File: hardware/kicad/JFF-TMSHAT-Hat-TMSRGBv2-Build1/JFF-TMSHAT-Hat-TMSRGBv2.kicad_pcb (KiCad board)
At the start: 2 copper layers, 56 x 73.5 mm, 15 parts, among them J1 TMSRGB-OUT, J13 AV EXT, J5 RGB, U100 TMS-RGB

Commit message: tmshats: add missing Y,R-Y,B-Y resistors
Signed-off-by: Albert Herranz <albert_herranz@yahoo.es>
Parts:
- added R16: 470, Resistor_SMD:R_0805_2012Metric_Pad1.20x1.40mm_HandSolder, F.Cu at (113.7, 122.5)
- added R17: 470, Resistor_SMD:R_0805_2012Metric_Pad1.20x1.40mm_HandSolder, F.Cu at (113.7, 120.0)
- added R18: 470, Resistor_SMD:R_0805_2012Metric_Pad1.20x1.40mm_HandSolder, F.Cu at (113.7, 127.5)
- moved SYM1 72.0 mm to (67.5, 75.2)
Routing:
- net AUDIO: track 95.5 -> 113.3 mm
- net COMVID/Y: track 35.0 -> 41.5 mm
- net EXTVDP/B-Y: track 35.0 -> 41.6 mm
- net CPUCLK/R-Y: track 44.2 -> 50.4 mm, vias 0 -> 1
- net GND: track 22.4 -> 18.9 mm, vias 2 -> 0

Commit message: tmshats: re-routed for enhanced reference plane
Signed-off-by: Albert Herranz <albert_herranz@yahoo.es>
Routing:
- net AUDIO: track 113.3 -> 83.4 mm, vias 0 -> 1
- net /AV: track 35.9 -> 51.8 mm, vias 1 -> 0
- net GND: track 18.9 -> 32.5 mm, vias 0 -> 7
- net /YS: track 40.1 -> 53.0 mm, vias 1 -> 0
- net +5V: track 65.5 -> 71.1 mm
- net SYNC_75: track 32.3 -> 30.8 mm

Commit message: tmshats: changed logos, minor routing change
Signed-off-by: Albert Herranz <albert_herranz@yahoo.es>
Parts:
- added G***: LOGO, My_Components:logo-hat, F.Cu at (112.4, 69.5)
- added G***: LOGO, My_Components:logo-tms, F.Cu at (112.4, 67.2)
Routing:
- net EXTVDP/B-Y: track 41.3 -> 40.6 mm

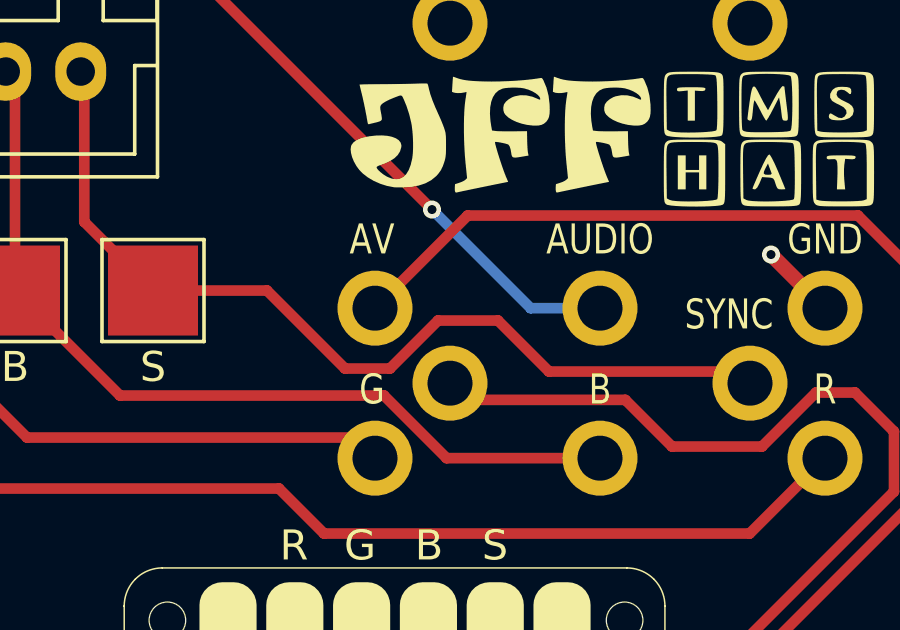
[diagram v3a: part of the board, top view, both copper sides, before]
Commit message: tmshats: add back missing YS silkscreen text
Signed-off-by: Albert Herranz <albert_herranz@yahoo.es>
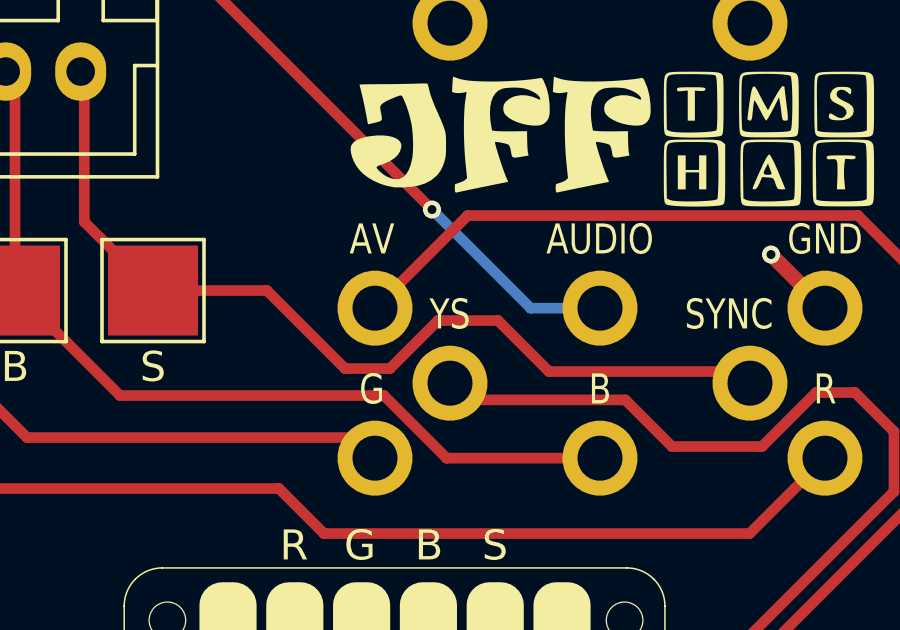
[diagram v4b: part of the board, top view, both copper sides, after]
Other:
- board text added: "YS"
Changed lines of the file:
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@@
+		)
+	)
+	(gr_text "YS"
+		(at 101.8 74.2 0)
+		(layer "F.SilkS")
+		(effects
+			(font
+				(size 1 0.8)
+				(thickness 0.2)
+			)
 		)
 	)
